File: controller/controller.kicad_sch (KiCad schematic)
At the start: 12 parts, among them J1 Conn_02x20_Odd_Even, SW1 SW_Push, SW2 SW_Push, SW3 SW_Push, SW4 SW_Push, SW5 SW_Push, SW6 SW_Push, SW7 SW_Push

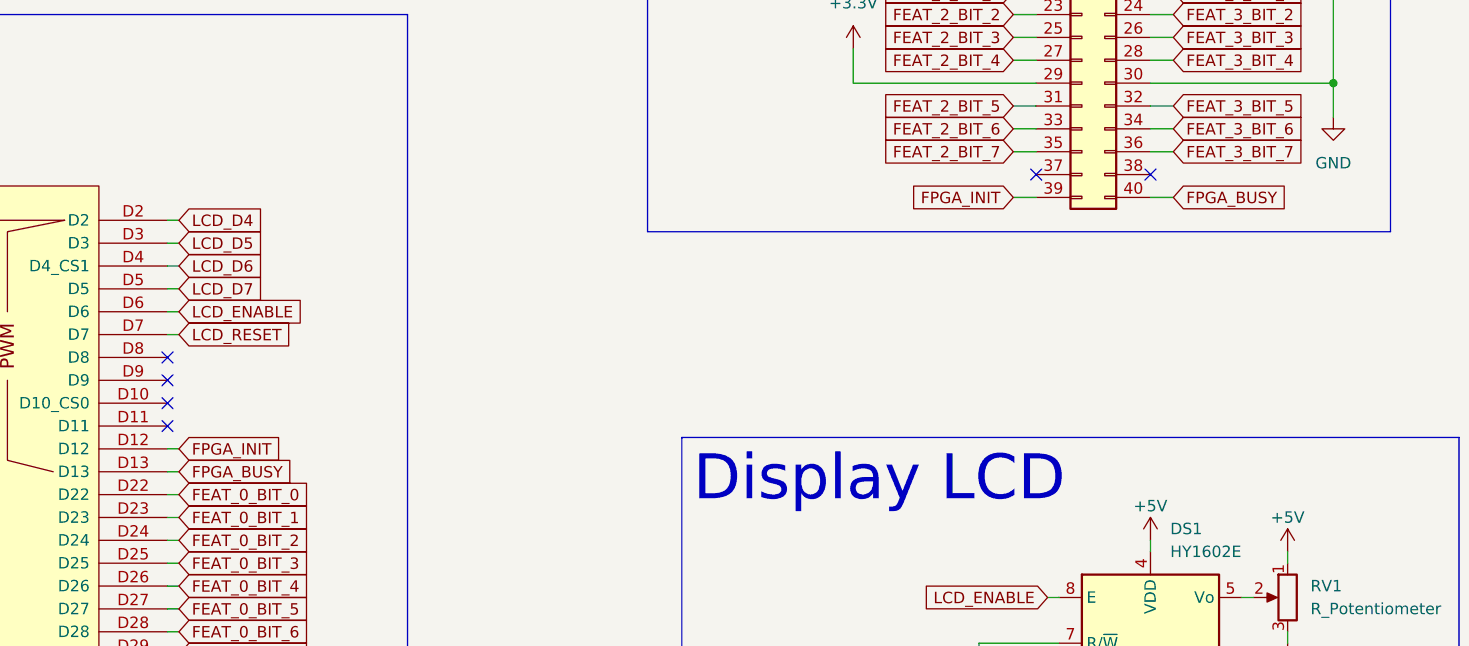
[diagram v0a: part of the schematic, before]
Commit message: Class output handle added
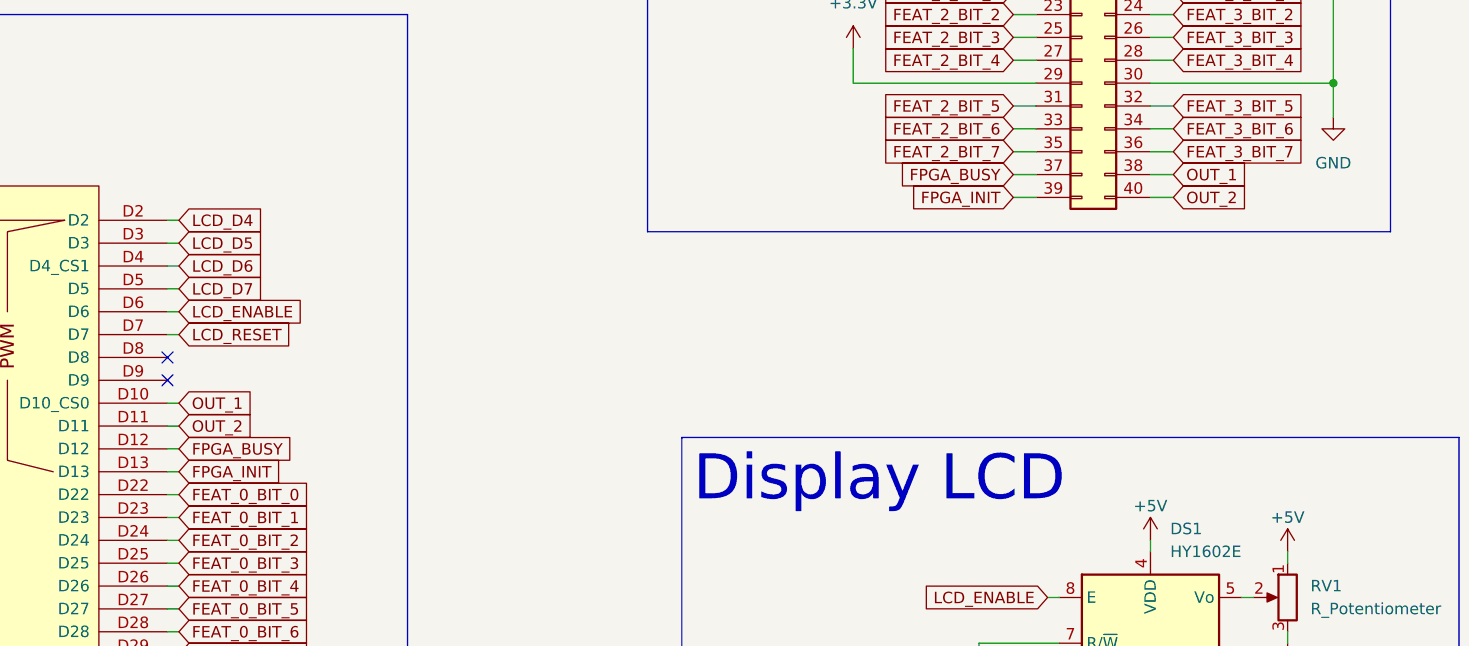
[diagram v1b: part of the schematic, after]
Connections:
- net FPGA_BUSY: now also A1.D12, J1.37 (Pin_37); no longer A1.D13, J1.40 (Pin_40)
- net FPGA_INIT: now also A1.D13; no longer A1.D12
- net OUT_1: now reaches A1.D10 (D10_CS0)
- net OUT_1: now also J1.38 (Pin_38)
- net OUT_2: now reaches A1.D11
- net OUT_2: now also J1.40 (Pin_40)
- no-connect marks 40 -> 36
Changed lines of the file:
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@@
   (no_connect (at 64.77 77.47))
   (no_connect (at 64.77 120.65))
-  (no_connect (at 130.81 97.79))
   (no_connect (at 229.87 134.62))
   (no_connect (at 130.81 92.71))
-  (no_connect (at 240.03 72.39))
   (no_connect (at 64.77 125.73))
   (no_connect (at 64.77 138.43))
@@
   (no_connect (at 130.81 95.25))
   (no_connect (at 64.77 95.25))
-  (no_connect (at 227.33 72.39))
   (no_connect (at 64.77 133.35))
   (no_connect (at 64.77 148.59))
   (no_connect (at 64.77 140.97))
-  (no_connect (at 130.81 100.33))
   (no_connect (at 64.77 115.57))
   (no_connect (at 64.77 128.27))
@@
     (stroke (width 0) (type default))
   )
+  (wire (pts (xy 130.81 102.87) (xy 132.08 102.87))
+    (stroke (width 0) (type default))
+  )
   (wire (pts (xy 240.03 64.77) (xy 242.57 64.77))
     (stroke (width 0) (type default))
@@
     (stroke (width 0) (type default))
   )
+  (wire (pts (xy 240.03 74.93) (xy 242.57 74.93))
+    (stroke (width 0) (type default))
+  )
   (wire (pts (xy 240.03 154.94) (xy 240.03 156.21))
     (stroke (width 0) (type default))
@@
     (stroke (width 0) (type default))
   )
+  (wire (pts (xy 130.81 100.33) (xy 132.08 100.33))
+    (stroke (width 0) (type default))
+  )
   (wire (pts (xy 264.16 134.62) (xy 264.16 130.81))
     (stroke (width 0) (type default))
@@
     (stroke (width 0) (type default))
   )
+  (wire (pts (xy 224.79 72.39) (xy 227.33 72.39))
+    (stroke (width 0) (type default))
+  )
   (wire (pts (xy 64.77 168.91) (xy 58.42 168.91))
     (stroke (width 0) (type default))
@@
     (stroke (width 0) (type default))
   )
+  (wire (pts (xy 130.81 105.41) (xy 132.08 105.41))
+    (stroke (width 0) (type default))
+  )
   (wire (pts (xy 58.42 176.53) (xy 58.42 179.07))
     (stroke (width 0) (type default))
@@
     (stroke (width 0) (type default))
   )
-  (wire (pts (xy 130.81 105.41) (xy 132.08 105.41))
-    (stroke (width 0) (type default))
-  )
   (wire (pts (xy 240.03 67.31) (xy 242.57 67.31))
     (stroke (width 0) (type default))
@@
     (stroke (width 0) (type default))
   )
-  (wire (pts (xy 130.81 102.87) (xy 132.08 102.87))
-    (stroke (width 0) (type default))
-  )
   (wire (pts (xy 30.48 35.56) (xy 30.48 38.1))
     (stroke (width 0) (type default))
@@
     (stroke (width 0) (type default))
   )
-  (wire (pts (xy 240.03 74.93) (xy 242.57 74.93))
-    (stroke (width 0) (type default))
-  )
   (wire (pts (xy 58.42 179.07) (xy 58.42 181.61))
     (stroke (width 0) (type default))
@@
     (stroke (width 0) (type default))
   )
+  (wire (pts (xy 240.03 72.39) (xy 242.57 72.39))
+    (stroke (width 0) (type default))
+  )
   (wire (pts (xy 64.77 181.61) (xy 58.42 181.61))
     (stroke (width 0) (type default))
@@
   )
   (wire (pts (xy 240.03 29.21) (xy 242.57 29.21))
+    (stroke (width 0) (type default))
+  )
+  (wire (pts (xy 130.81 97.79) (xy 132.08 97.79))
     (stroke (width 0) (type default))
   )
@@
     )
   )
-  (global_label "FPGA_BUSY" (shape input) (at 242.57 74.93 0) (fields_autoplaced)
-    (effects (font (size 1.27 1.27)) (justify left))
-    (property "Intersheetrefs" "${INTERSHEET_REFS}" (at 256.1386 74.93 0)
-      (effects (font (size 1.27 1.27)) (justify left) hide)
+  (global_label "FPGA_BUSY" (shape input) (at 224.79 72.39 180) (fields_autoplaced)
+    (effects (font (size 1.27 1.27)) (justify right))
+    (property "Intersheetrefs" "${INTERSHEET_REFS}" (at 211.2214 72.39 0)
+      (effects (font (size 1.27 1.27)) (justify right) hide)
     )
   )
@@
     )
   )
+  (global_label "OUT_2" (shape input) (at 242.57 74.93 0) (fields_autoplaced)
+    (effects (font (size 1.27 1.27)) (justify left))
+    (property "Intersheetrefs" "${INTERSHEET_REFS}" (at 251.3609 74.93 0)
+      (effects (font (size 1.27 1.27)) (justify left) hide)
+    )
+  )
   (global_label "FEAT_1_BIT_5" (shape input) (at 242.57 41.91 0) (fields_autoplaced)
     (effects (font (size 1.27 1.27)) (justify left))
@@
     )
   )
+  (global_label "OUT_2" (shape input) (at 132.08 100.33 0) (fields_autoplaced)
+    (effects (font (size 1.27 1.27)) (justify left))
+    (property "Intersheetrefs" "${INTERSHEET_REFS}" (at 140.8709 100.33 0)
+      (effects (font (size 1.27 1.27)) (justify left) hide)
+    )
+  )
   (global_label "FEAT_3_BIT_4" (shape input) (at 132.08 179.07 0) (fields_autoplaced)
     (effects (font (size 1.27 1.27)) (justify left))
@@
     )
   )
+  (global_label "OUT_1" (shape input) (at 242.57 72.39 0) (fields_autoplaced)
+    (effects (font (size 1.27 1.27)) (justify left))
+    (property "Intersheetrefs" "${INTERSHEET_REFS}" (at 251.3609 72.39 0)
+      (effects (font (size 1.27 1.27)) (justify left) hide)
+    )
+  )
   (global_label "FEAT_0_BIT_4" (shape input) (at 132.08 118.11 0) (fields_autoplaced)
     (effects (font (size 1.27 1.27)) (justify left))
@@
     )
   )
-  (global_label "FPGA_INIT" (shape input) (at 132.08 102.87 0) (fields_autoplaced)
-    (effects (font (size 1.27 1.27)) (justify left))
-    (property "Intersheetrefs" "${INTERSHEET_REFS}" (at 144.2577 102.87 0)
+  (global_label "FPGA_INIT" (shape input) (at 132.08 105.41 0) (fields_autoplaced)
+    (effects (font (size 1.27 1.27)) (justify left))
+    (property "Intersheetrefs" "${INTERSHEET_REFS}" (at 144.2577 105.41 0)
       (effects (font (size 1.27 1.27)) (justify left) hide)
     )
@@
     )
   )
+  (global_label "OUT_1" (shape input) (at 132.08 97.79 0) (fields_autoplaced)
+    (effects (font (size 1.27 1.27)) (justify left))
+    (property "Intersheetrefs" "${INTERSHEET_REFS}" (at 140.8709 97.79 0)
+      (effects (font (size 1.27 1.27)) (justify left) hide)
+    )
+  )
   (global_label "LCD_RESET" (shape input) (at 226.06 127 270) (fields_autoplaced)
     (effects (font (size 1.27 1.27)) (justify right))
@@
     )
   )
-  (global_label "FPGA_BUSY" (shape input) (at 132.08 105.41 0) (fields_autoplaced)
-    (effects (font (size 1.27 1.27)) (justify left))
-    (property "Intersheetrefs" "${INTERSHEET_REFS}" (at 145.6486 105.41 0)
-      (effects (font (size 1.27 1.27)) (justify left) hide)
-    )
+  (global_label "FPGA_BUSY" (shape input) (at 132.08 102.87 0) (fields_autoplaced)
+    (effects (font (size 1.27 1.27)) (justify left))
+    (property "Intersheetrefs" "${INTERSHEET_REFS}" (at 145.6486 102.87 0)
+      (effects (font (size 1.27 1.27)) (justify left) hide)
+    )
